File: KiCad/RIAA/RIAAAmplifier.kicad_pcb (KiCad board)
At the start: 2 copper layers, 60 x 37 mm, 71 parts, among them J1 RND 205-00698, J2 RND 205-00699, J3 JST_PH_B3B-PH-K, J4 RND 205-00698, J5 RND 205-00699, J6 JST_PH_S3B-PH-K, U1 LT1115, U2 AD797, U3 AD797, U4 LT1115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

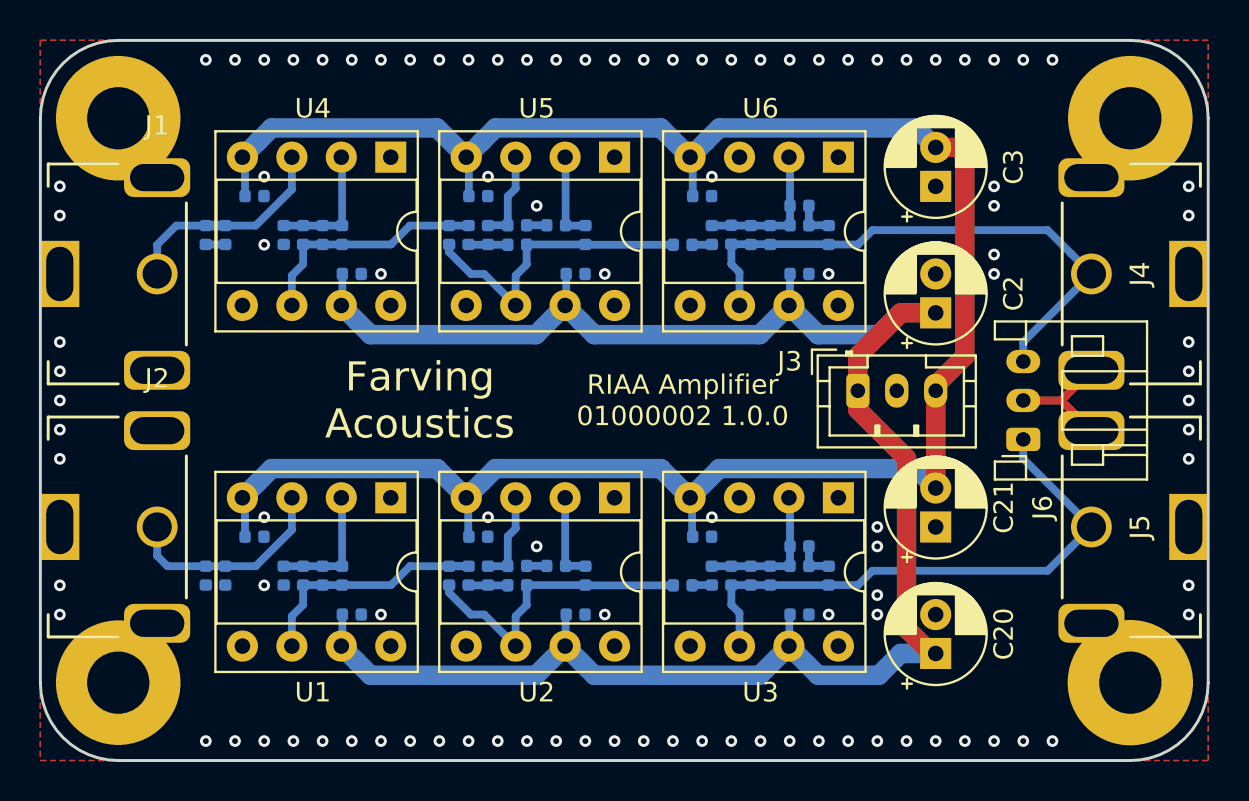
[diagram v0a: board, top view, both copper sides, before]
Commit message: Update OpAmp to KiCad Library symbol
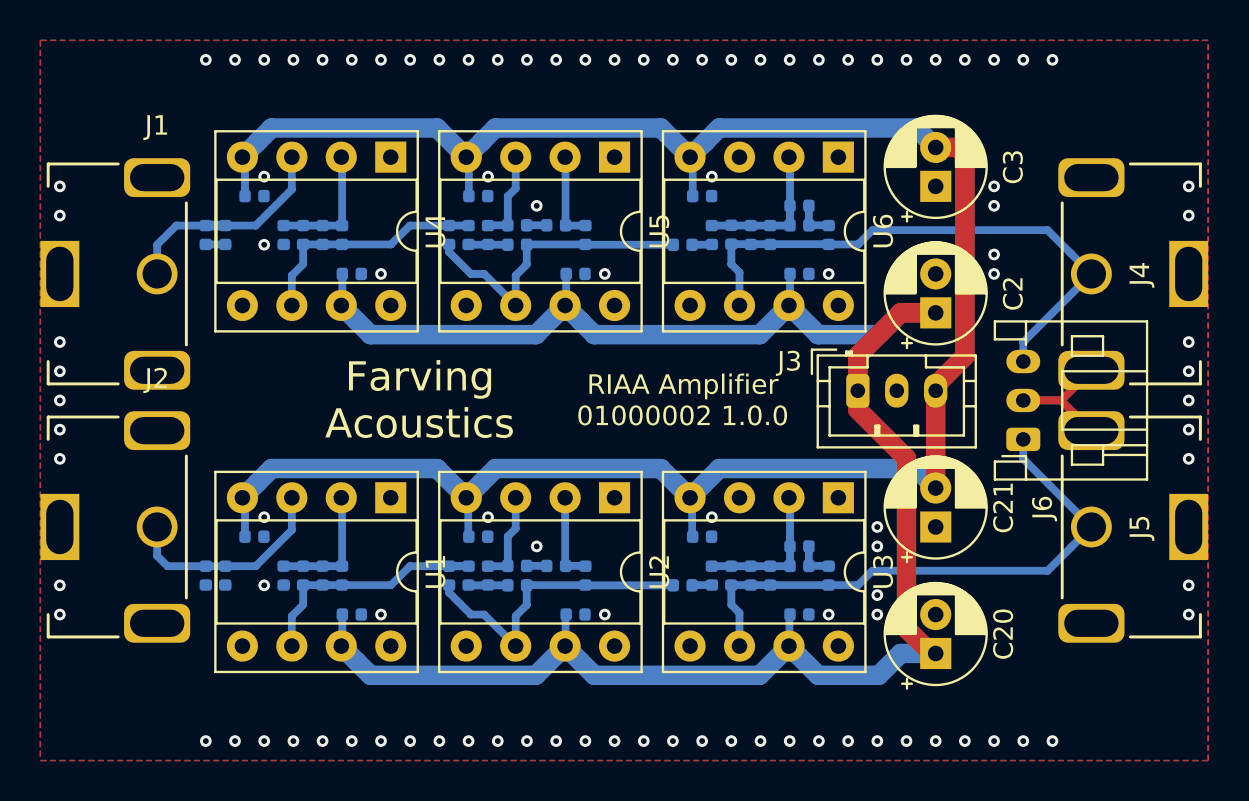
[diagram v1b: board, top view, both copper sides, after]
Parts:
- removed PCB1: Board_Module, PCB:PCB_Board_60x37
- C7, C8: value 3n3 -> 3.3n
- R11, R19, R21, R24, R6, R8: value 4k7 -> 4.7k
- R17, R4: value 2k4 -> 2.4k
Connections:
- U1 pad 1: (no net) -> Net-(U1-Pad1)
- U1 pad 5: (no net) -> Net-(U1-Pad5)
- U1 pad 8: (no net) -> Net-(U1-Pad8)
- U2 pad 1: (no net) -> Net-(U2-Pad1)
- U2 pad 5: (no net) -> Net-(U2-Pad5)
- U2 pad 8: (no net) -> Net-(U2-Pad8)
- U3 pad 1: (no net) -> Net-(U3-Pad1)
- U3 pad 5: (no net) -> Net-(U3-Pad5)
- U3 pad 8: (no net) -> Net-(U3-Pad8)
- U4 pad 1: (no net) -> Net-(U4-Pad1)
- U4 pad 5: (no net) -> Net-(U4-Pad5)
- U4 pad 8: (no net) -> Net-(U4-Pad8)
- U5 pad 1: (no net) -> Net-(U5-Pad1)
- U5 pad 5: (no net) -> Net-(U5-Pad5)
- U5 pad 8: (no net) -> Net-(U5-Pad8)
- U6 pad 1: (no net) -> Net-(U6-Pad1)
- U6 pad 5: (no net) -> Net-(U6-Pad5)
- U6 pad 8: (no net) -> Net-(U6-Pad8)
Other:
- board outline removed
